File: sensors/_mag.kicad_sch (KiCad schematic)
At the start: 4 parts, among them U4 IST8310

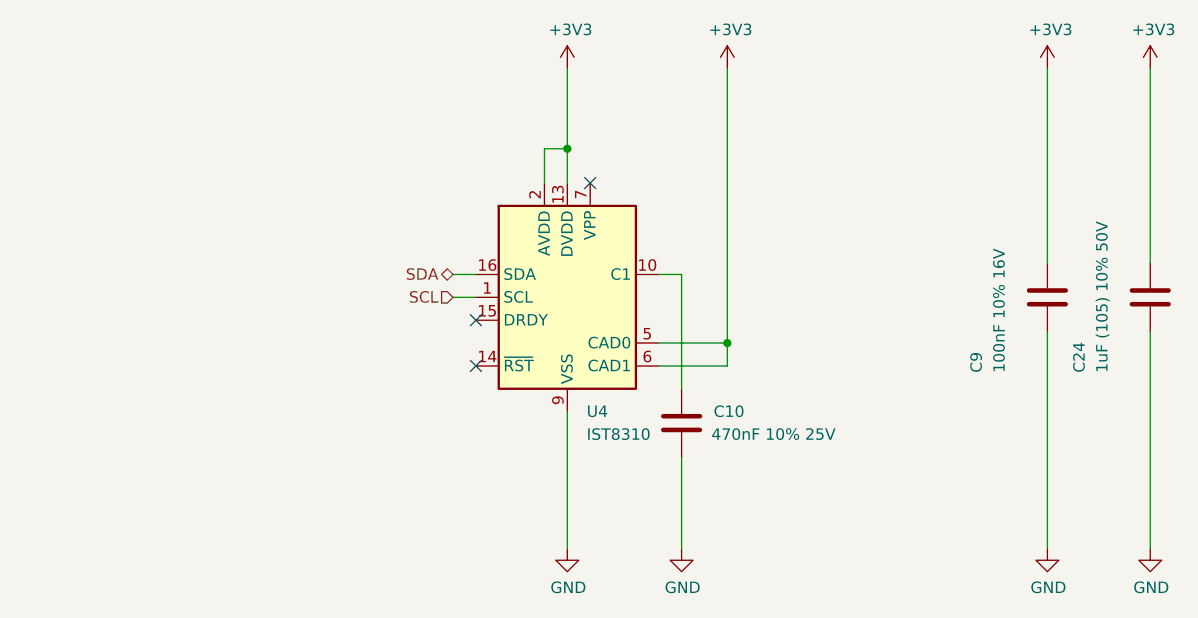
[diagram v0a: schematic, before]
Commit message: replace magnetometer IST8310 -> MMC5983MA
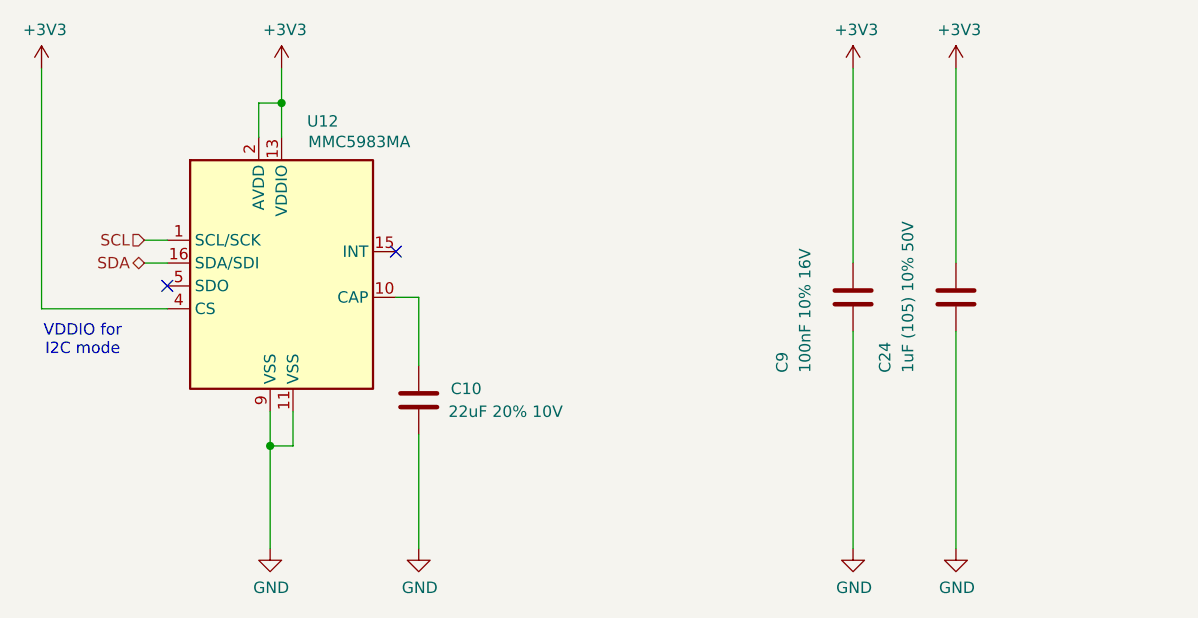
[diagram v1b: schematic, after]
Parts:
- removed U4: IST8310, Package_LGA:LGA-16_3x3mm_P0.5mm, symbol Sensor_Magnetic:IST8310
- added U12: MMC5983MA, Package_LGA:LGA-16_3x3mm_P0.5mm, symbol pilotpi:MMC5983MA
- C10: value 470nF 10% 25V -> 22uF 20% 10V; footprint Capacitor_SMD:C_0603_1608Metric -> Capacitor_SMD:C_0805_2012Metric; Part CL10B474KA8NNNC -> GRM21BZ71A226ME15L
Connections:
- net +3V3: now also U12.13 (VDDIO), U12.2 (AVDD), U12.4 (CS)
- net GND: now also U12.11 (VSS), U12.9 (VSS)
- net SCL: now also U12.1 (SCL/SCK)
- net SDA: now also U12.16 (SDA/SDI)
- net at C10.1: now also U12.10 (CAP)
- no-connect marks 3 -> 2
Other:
- note added: "VDDIO for I2C mode"
- moved on the sheet: C10, C24, C9

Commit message: add part number
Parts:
- U12: Part (none) -> MMC5983MA
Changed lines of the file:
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@@
+			)
+		)
+		(property "Part" "MMC5983MA"
+			(at 114.3 90.17 0)
+			(hide yes)
+			(show_name no)
+			(do_not_autoplace no)
+			(effects
+				(font
+					(size 1.27 1.27)
+				)
 			)
 		)
